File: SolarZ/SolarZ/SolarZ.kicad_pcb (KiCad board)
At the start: 4 copper layers, 99 x 99 mm, 47 parts, among them X1 BU-SMA-V

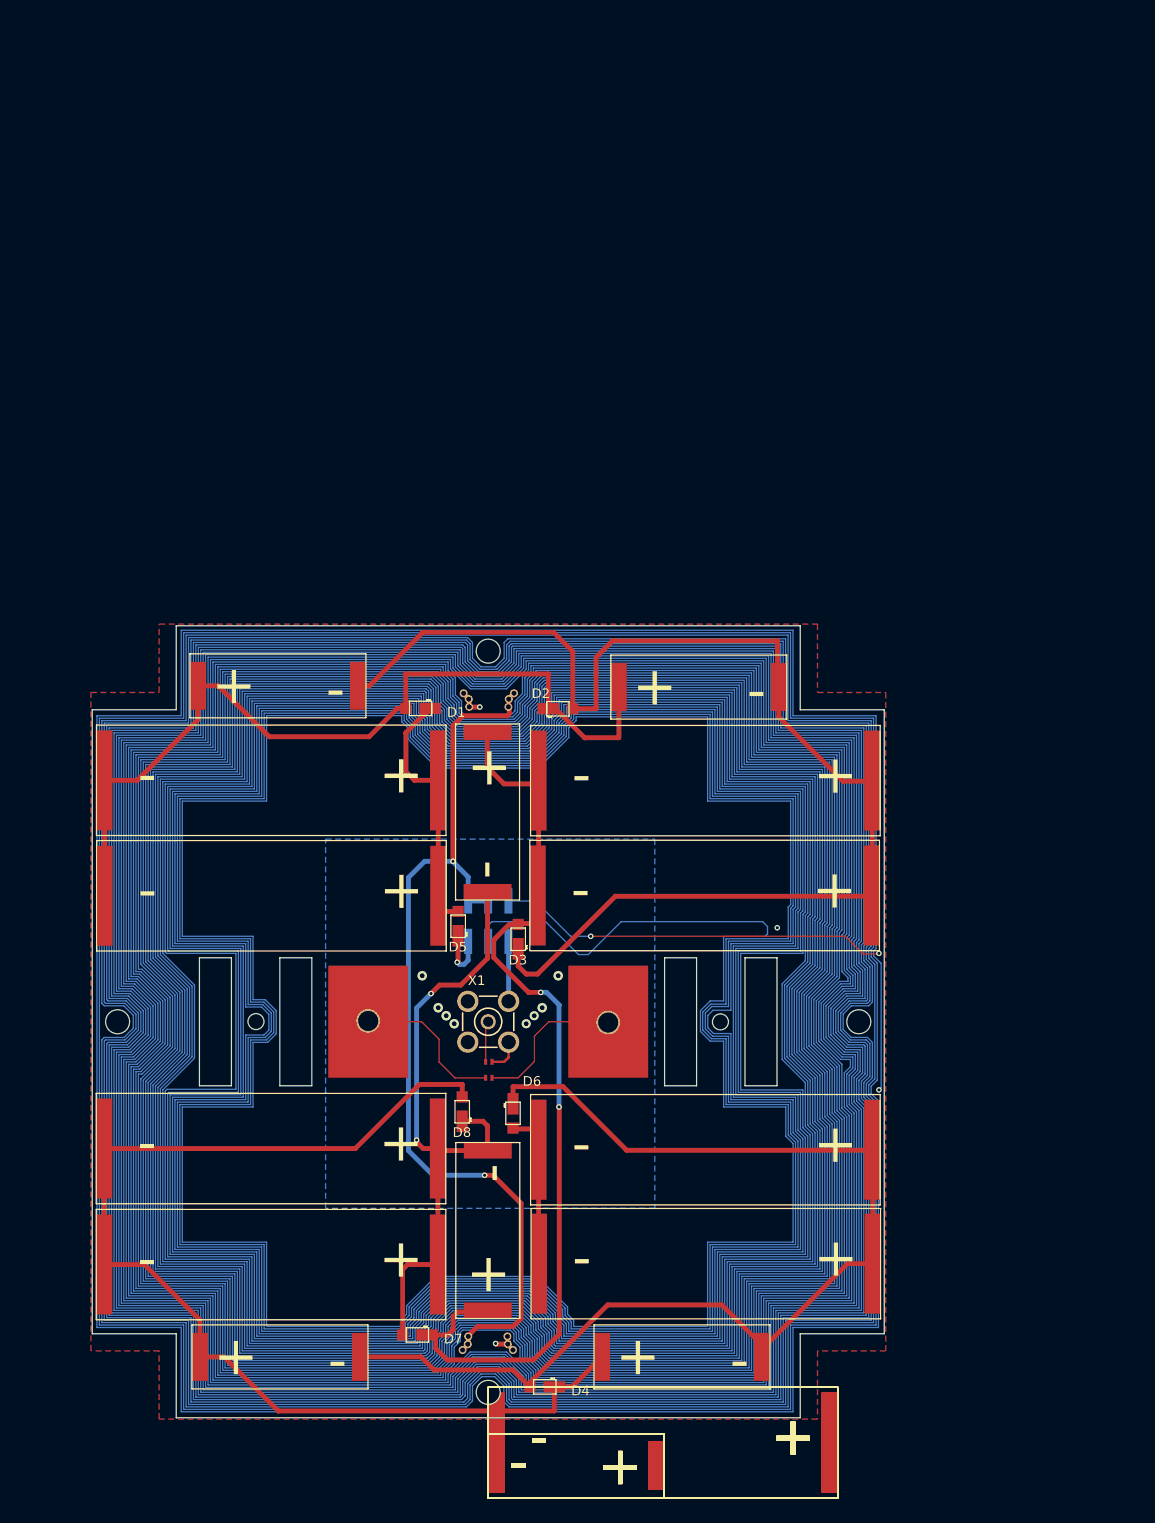
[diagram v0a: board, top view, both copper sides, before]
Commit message: Preliminary layout, pending updates from AV about radio.
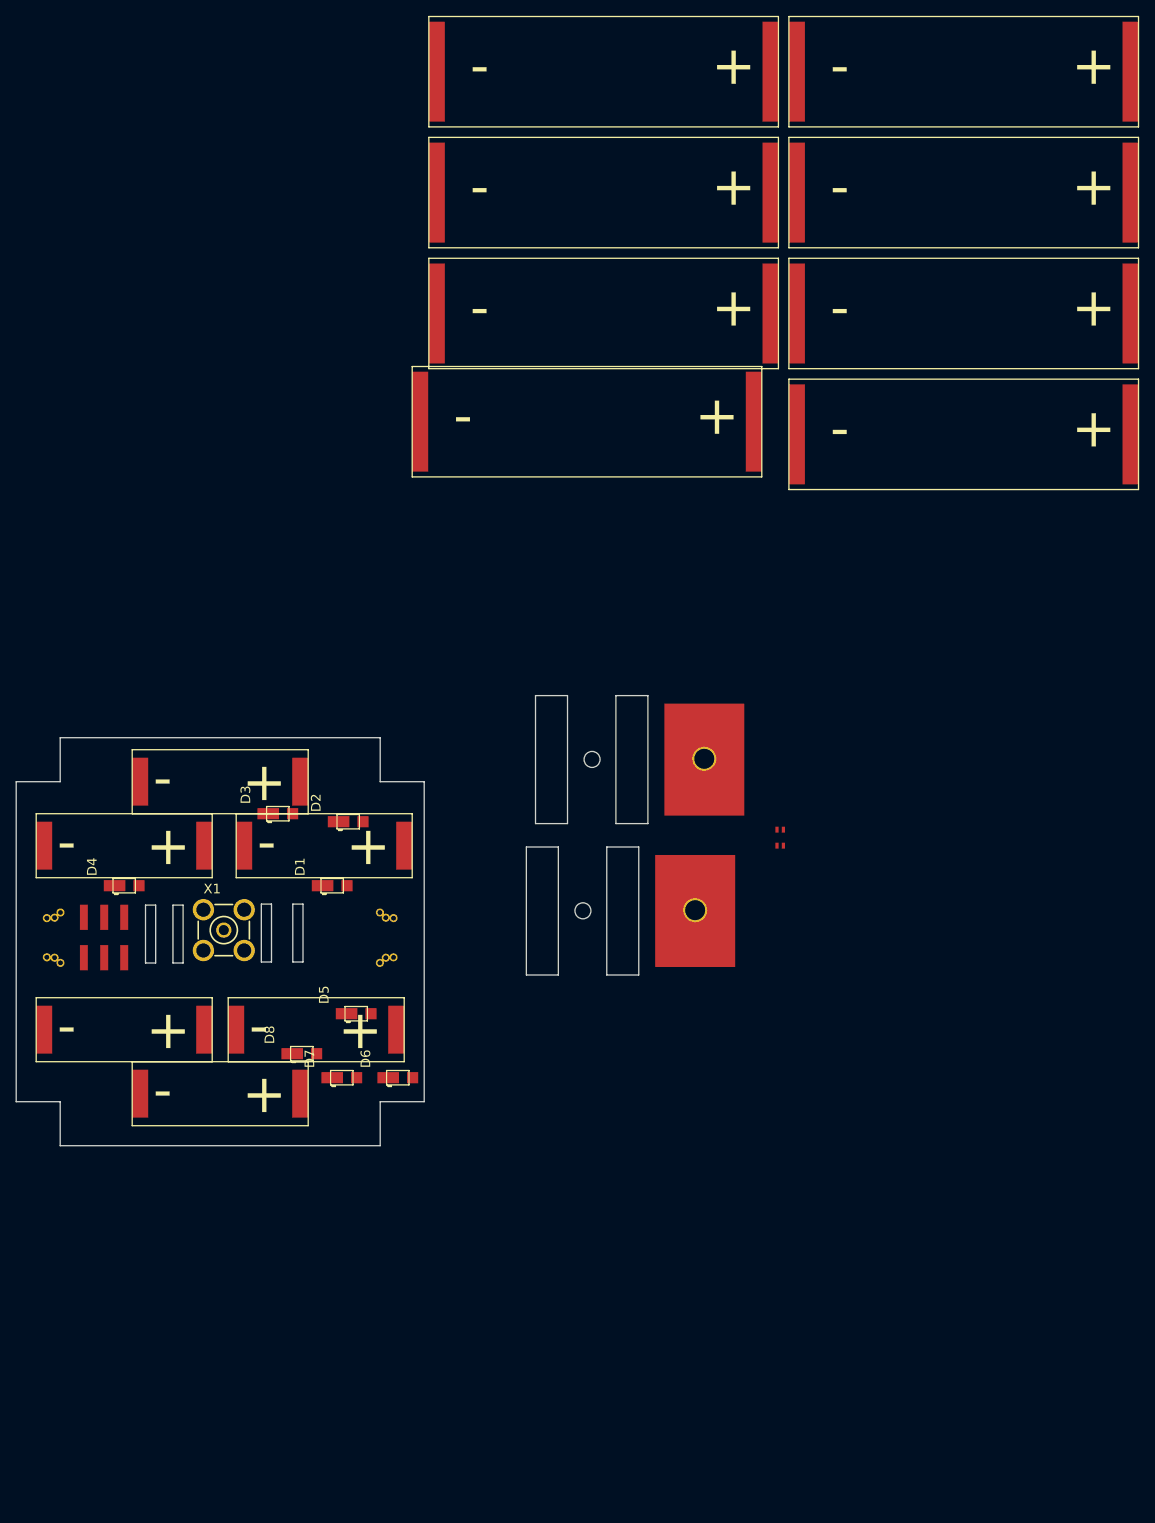
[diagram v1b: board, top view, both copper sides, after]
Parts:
- removed 1, 10, 11, 13, 6, 7: KXOB22-04X3F, SolarZ:KXOB22-04X3F
- removed 12, 14, 2, 3, 4, 5, 8, 9: SLMD121H04L, SolarZ:SLMD121H04L
- removed @HOLE0, @HOLE1, @HOLE2, @HOLE3: , 
- U$4: moved to F.Cu
- moved UNK2 175.4 mm to (186.1, -6.85)
- moved UNK14 171.5 mm to (141.1, -6.85)
- moved UNK9 160.7 mm to (186.1, 8.26)
- moved UNK12 156.4 mm to (141.1, 8.26)
- moved UNK4 146.1 mm to (186.1, 23.4)
- moved UNK3 141.3 mm to (141.1, 23.4)
- moved UNK5 131.5 mm to (186.1, 38.5)
- moved UNK8 128.0 mm to (139.0, 36.9)
- moved UNK11 96.4 mm to (104.0, 79.0)
- moved UNK7 95.9 mm to (92.0, 87.0)
- moved UNK1 83.7 mm to (117.0, 87.0)
- moved D4 81.8 mm to (103.0, 88.0), turned to 0 degrees
- moved UNK13 78.5 mm to (92.0, 110.0)
- moved UNK10 64.4 mm to (104.0, 118.0)
- moved UNK6 63.5 mm to (116.0, 110.0)
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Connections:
- U$1 pad 4: Net-(U$1-Pad4) -> (no net)
- X1 pad 1: Net-(X1-Pad1) -> (no net)
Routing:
- net Net-(U$4-PadP$2): track 41462.7 -> 0.00 mm, vias 4 -> 0
- net (no net): track 0.00 -> 411.3 mm
- net Net-(D2-PadPOS): track 160.5 -> 0.00 mm
- net Net-(D4-PadPOS): track 143.8 -> 0.00 mm
- net Net-(D4-PadNEG): track 141.2 -> 0.00 mm
- net Net-(D3-PadPOS): track 118.9 -> 0.00 mm, vias 2 -> 0
- net Net-(F1-Pad1): track 118.1 -> 0.00 mm, vias 2 -> 0
- net Net-(D1-PadPOS): track 106.7 -> 0.00 mm
- net Net-(D7-PadPOS): track 79.7 -> 0.00 mm, vias 2 -> 0
- net GND: track 39.6 -> 0.00 mm, vias 10 -> 0
- net Net-(D1-PadNEG): track 32.4 -> 0.00 mm
- net Net-(U$1-Pad1): track 19.4 -> 0.00 mm
- net Net-(U$1-Pad2): track 19.4 -> 0.00 mm
- net /VSOLAR: track 7.40 -> 0.00 mm, vias 1 -> 0
- net Net-(X1-Pad1): track 5.14 -> 0.00 mm
- removed copper zone on B.Cu, net GND
- removed copper zone on F.Cu, net GND
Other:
- board size 99 x 99 mm -> 51 x 51 mm
- board text removed: "BW"
- board text removed: "GND"
- board text removed: "MT+"
- board text removed: "MT-"
- board text removed: "Solar Panel Z Rev B"
- board text removed: "VS"
